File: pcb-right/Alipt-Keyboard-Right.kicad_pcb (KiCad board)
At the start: 2 copper layers, 195 x 119.6 mm, 88 parts, among them J1 LED, J2 4PIN, J3 OLED, P1 i2c_pin, P2 i2c_pin, SW0 SW_PUSH, SW1 SW_PUSH, SW10 SW_PUSH, SW11 SW_PUSH, SW12 SW_PUSH, SW131 SW_PUSH, SW132 SW_PUSH, SW14 SW_PUSH, SW15 SW_PUSH, SW16 SW_PUSH, SW17 SW_PUSH, SW18 SW_PUSH, SW19 SW_PUSH, SW2 SW_PUSH, SW20 SW_PUSH, SW21 SW_PUSH, SW22 SW_PUSH, SW23 SW_PUSH, SW24 SW_PUSH, SW25 SW_PUSH, SW26 SW_PUSH, SW27 SW_PUSH, SW28 SW_PUSH, SW29 SW_PUSH, SW3 SW_PUSH, SW30 SW_PUSH, SW31 SW_PUSH, SW32 SW_PUSH, SW33 SW_PUSH, SW34 Rotary_Encoder_Switch, SW4 SW_PUSH, SW5 SW_PUSH, SW6 SW_PUSH, SW7 SW_PUSH, SW8 SW_PUSH, SW9 SW_PUSH, U1 ProMicro

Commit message: revision 1 complete pcbs
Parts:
- W1: moved to B.Cu
- moved D3 155.5 mm to (138.9, 63.2), turned to 102 degrees
- moved D21 149.5 mm to (79.9, 129.2), turned to 102 degrees
- moved D33 141.4 mm to (202.7, 99.6), turned to 90 degrees
- moved D32 140.6 mm to (226.4, 118.6), turned to 90 degrees
- moved D15 139.8 mm to (105.0, 109.5), turned to 102 degrees
- moved D13 139.2 mm to (234.3, 61.6), turned to 90 degrees
- moved D2 138.0 mm to (120.3, 67.1), turned to 102 degrees
- moved D6 136.6 mm to (196.1, 61.1), turned to 90 degrees
- moved D8 133.5 mm to (96.5, 91.8), turned to 104 degrees
- moved D4 132.2 mm to (158.5, 59.2), turned to 90 degrees
- moved D1 131.9 mm to (101.7, 71.1), turned to 102 degrees
- moved D14 131.0 mm to (86.6, 114.4), turned to 102 degrees
- moved D11 130.7 mm to (153.2, 79.3), turned to 90 degrees
- moved D5 129.4 mm to (177.5, 61.3), turned to 90 degrees
- moved D27 127.8 mm to (213.6, 80.5), turned to 90 degrees
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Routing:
- net row4: track 61.2 -> 330.1 mm
- net col0: track 51.4 -> 283.1 mm
- net col2: track 55.2 -> 277.0 mm, vias 2 -> 3
- net col1: track 73.9 -> 287.3 mm, vias 2 -> 3
- net row3: track 66.4 -> 267.8 mm, vias 1 -> 2
- net col3: track 99.4 -> 292.6 mm, vias 2 -> 3
- net row1: track 71.0 -> 247.9 mm
- net row2: track 68.4 -> 217.5 mm
- net row0: track 68.1 -> 183.5 mm
- net col4: track 141.0 -> 212.9 mm, vias 2 -> 3
- net col5: track 159.8 -> 190.8 mm
- net SW34A: track 222.4 -> 196.3 mm, vias 4 -> 3
- net Net-(D13-Pad2): track 0.00 -> 23.0 mm
- net Net-(D28-Pad2): track 0.00 -> 18.5 mm
- net Net-(D33-Pad2): track 0.00 -> 14.8 mm
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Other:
- board size 195 x 119.6 mm -> 197.4 x 119.6 mm

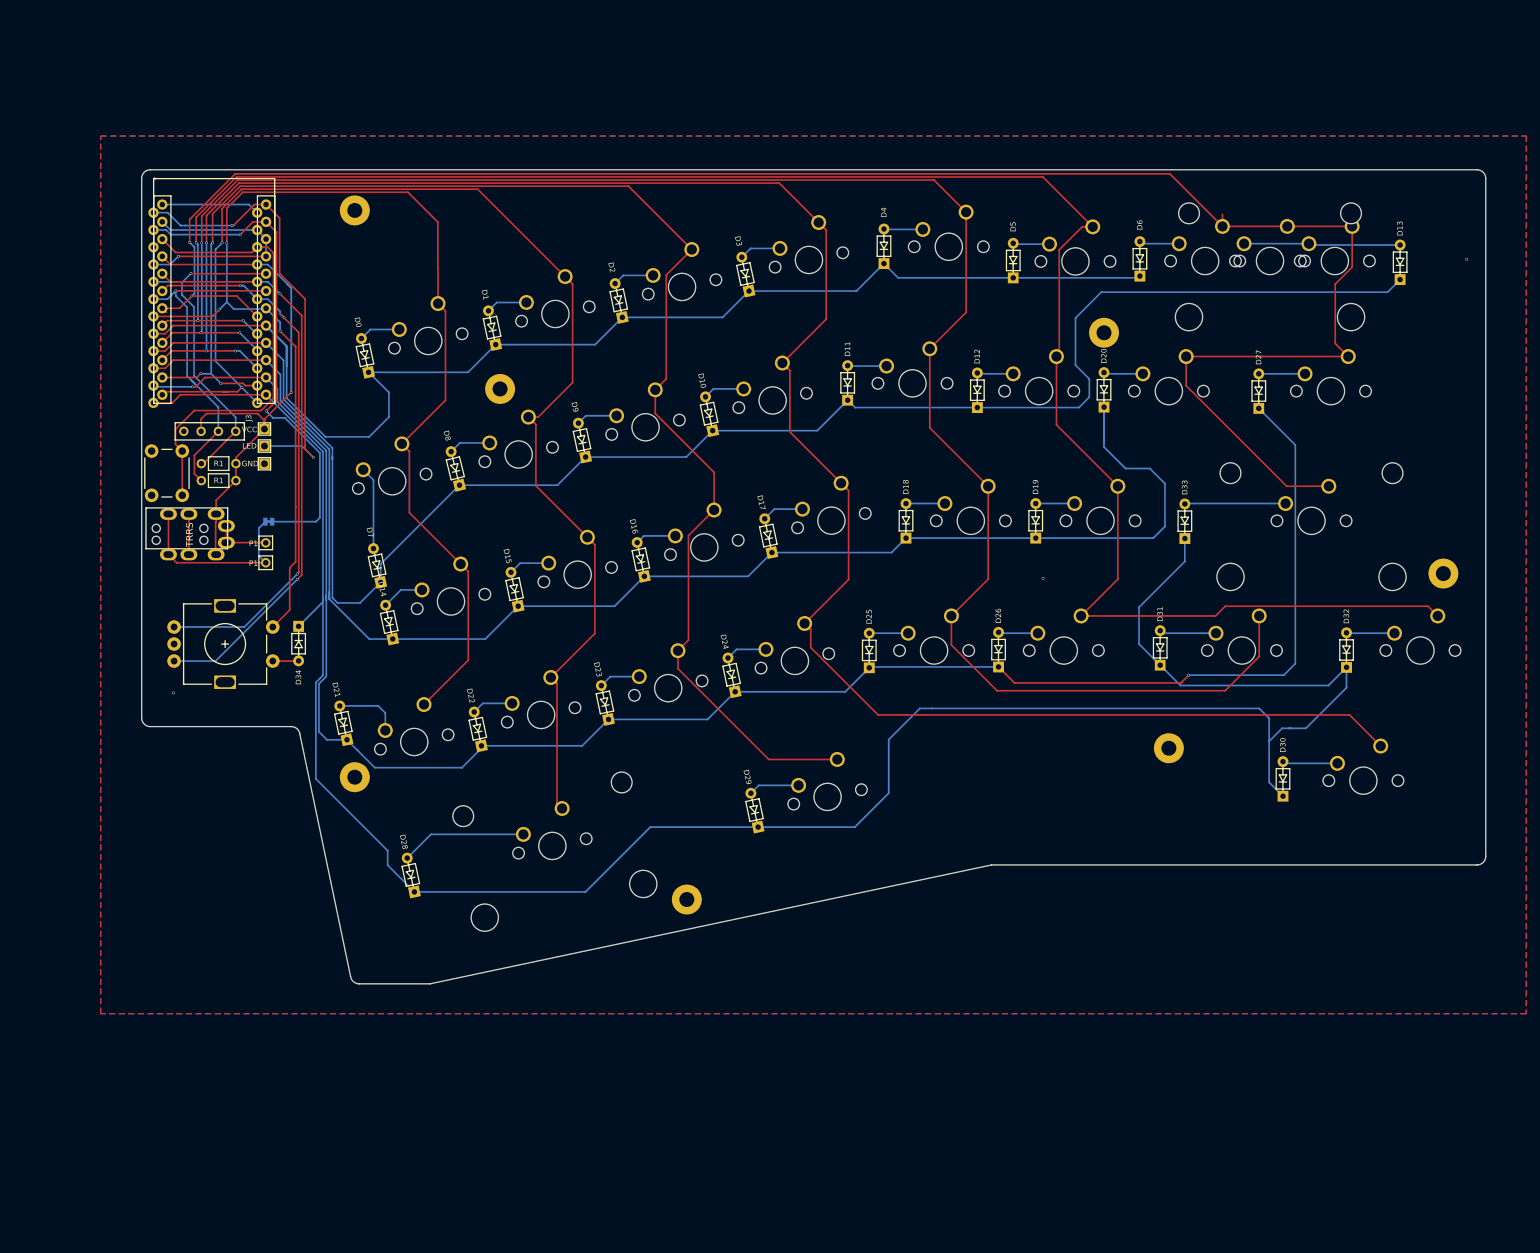
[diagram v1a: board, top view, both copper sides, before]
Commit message: Revision 2 PCB Changes
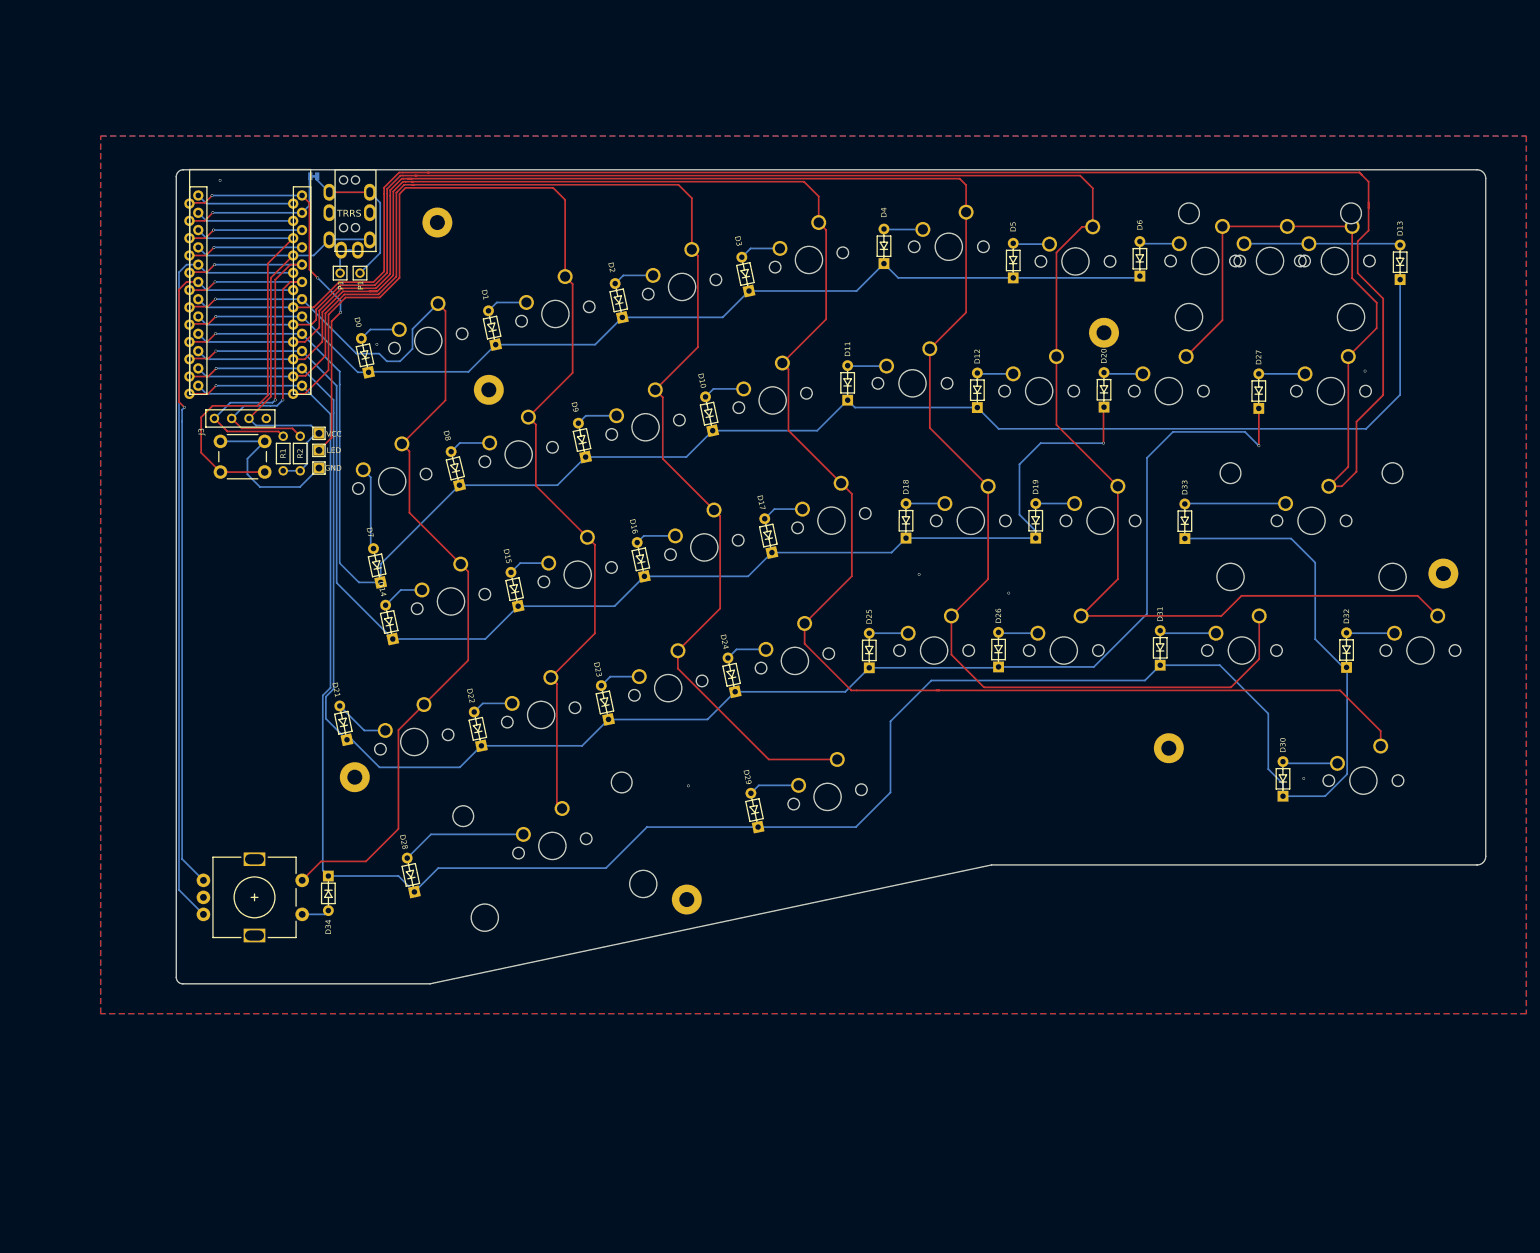
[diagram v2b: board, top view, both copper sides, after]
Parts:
- J1: moved to B.Cu
- R2: moved to F.Cu
- moved J2 61.7 mm to (79.1, 44.2), turned to 180 degrees
- moved W1 51.2 mm to (74.7, 45.1), turned to 0 degrees
- moved P2 44.7 mm to (81.5, 59.4), turned to 270 degrees
- moved P1 41.1 mm to (78.6, 59.4), turned to 270 degrees
- moved SW34 37.5 mm to (66.0, 151.1)
- moved D34 36.9 mm to (76.9, 146.7)
- moved RSW1 12.8 mm to (61.0, 84.1), turned to 0 degrees
- moved R2 12.6 mm to (72.8, 85.9), turned to 90 degrees
- moved TH1 12.3 mm to (92.9, 51.9)
- moved R1 9.60 mm to (70.3, 85.9), turned to 90 degrees
- moved J1 8.03 mm to (75.5, 82.9), turned to 180 degrees
- moved U1 5.45 mm to (64.2, 62.7)
- moved J3 3.65 mm to (60.1, 80.7), turned to 0 degrees
- moved TH6 1.66 mm to (100.5, 76.5)
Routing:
- net DATA: track 73.9 -> 22.9 mm, vias 2 -> 1
- net SW34A: track 196.3 -> 151.8 mm, vias 3 -> 1
- net col0: track 283.1 -> 324.2 mm, vias 2 -> 0
- net row0: track 183.5 -> 151.1 mm, vias 0 -> 1
- net GND: track 44.6 -> 73.7 mm, vias 5 -> 9
- net ENCA: track 85.1 -> 113.5 mm, vias 2 -> 0
- net ENCB: track 81.2 -> 106.3 mm, vias 3 -> 1
- net row2: track 217.5 -> 196.5 mm, vias 0 -> 2
- net row3: track 267.8 -> 251.4 mm
- net col2: track 277.0 -> 265.1 mm, vias 3 -> 0
- net SDA: track 49.3 -> 60.8 mm, vias 1 -> 2
- net col5: track 190.8 -> 179.6 mm, vias 2 -> 0
- net col1: track 287.3 -> 276.8 mm, vias 3 -> 0
- net col3: track 292.6 -> 282.9 mm, vias 3 -> 0
- net LED: track 67.5 -> 58.6 mm, vias 2 -> 3
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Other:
- board size 197.4 x 119.6 mm -> 192.3 x 119.6 mm
